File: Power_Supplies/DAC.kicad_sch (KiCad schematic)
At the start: 42 parts, among them J1 Line Out, J2 Headphone Out, U10 OPA2134, U11 TPA6110A2DGN, U9 PCM1780

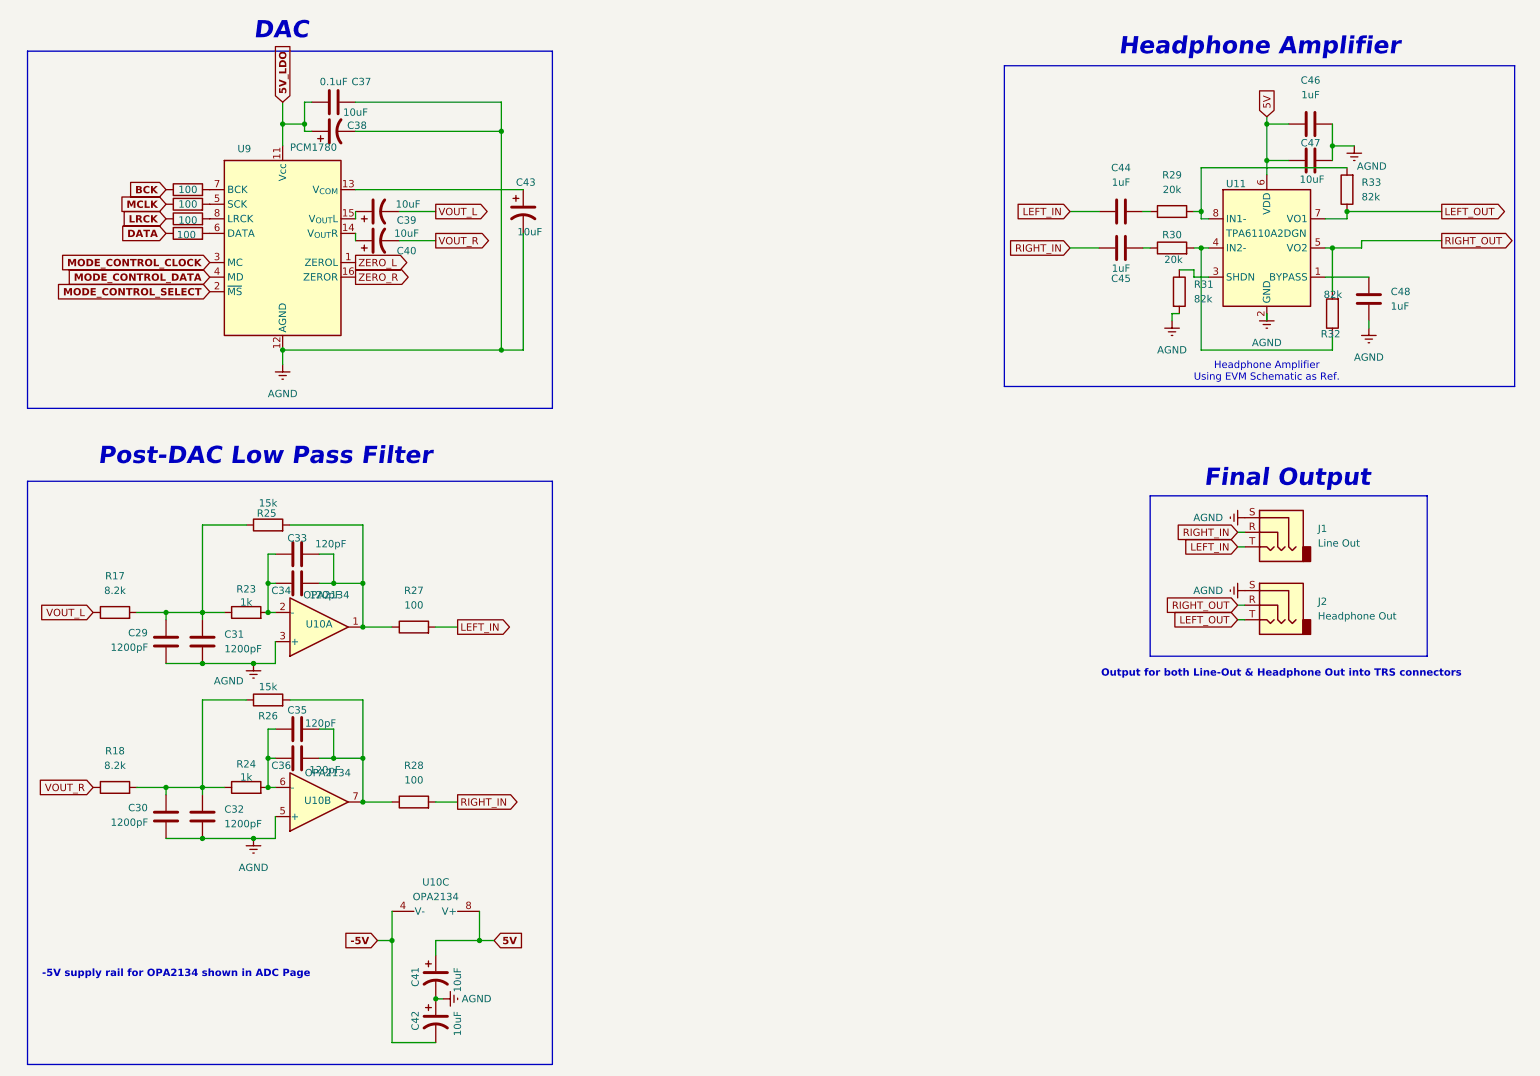
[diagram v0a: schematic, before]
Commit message: added both ADCs, added differential output to DACs
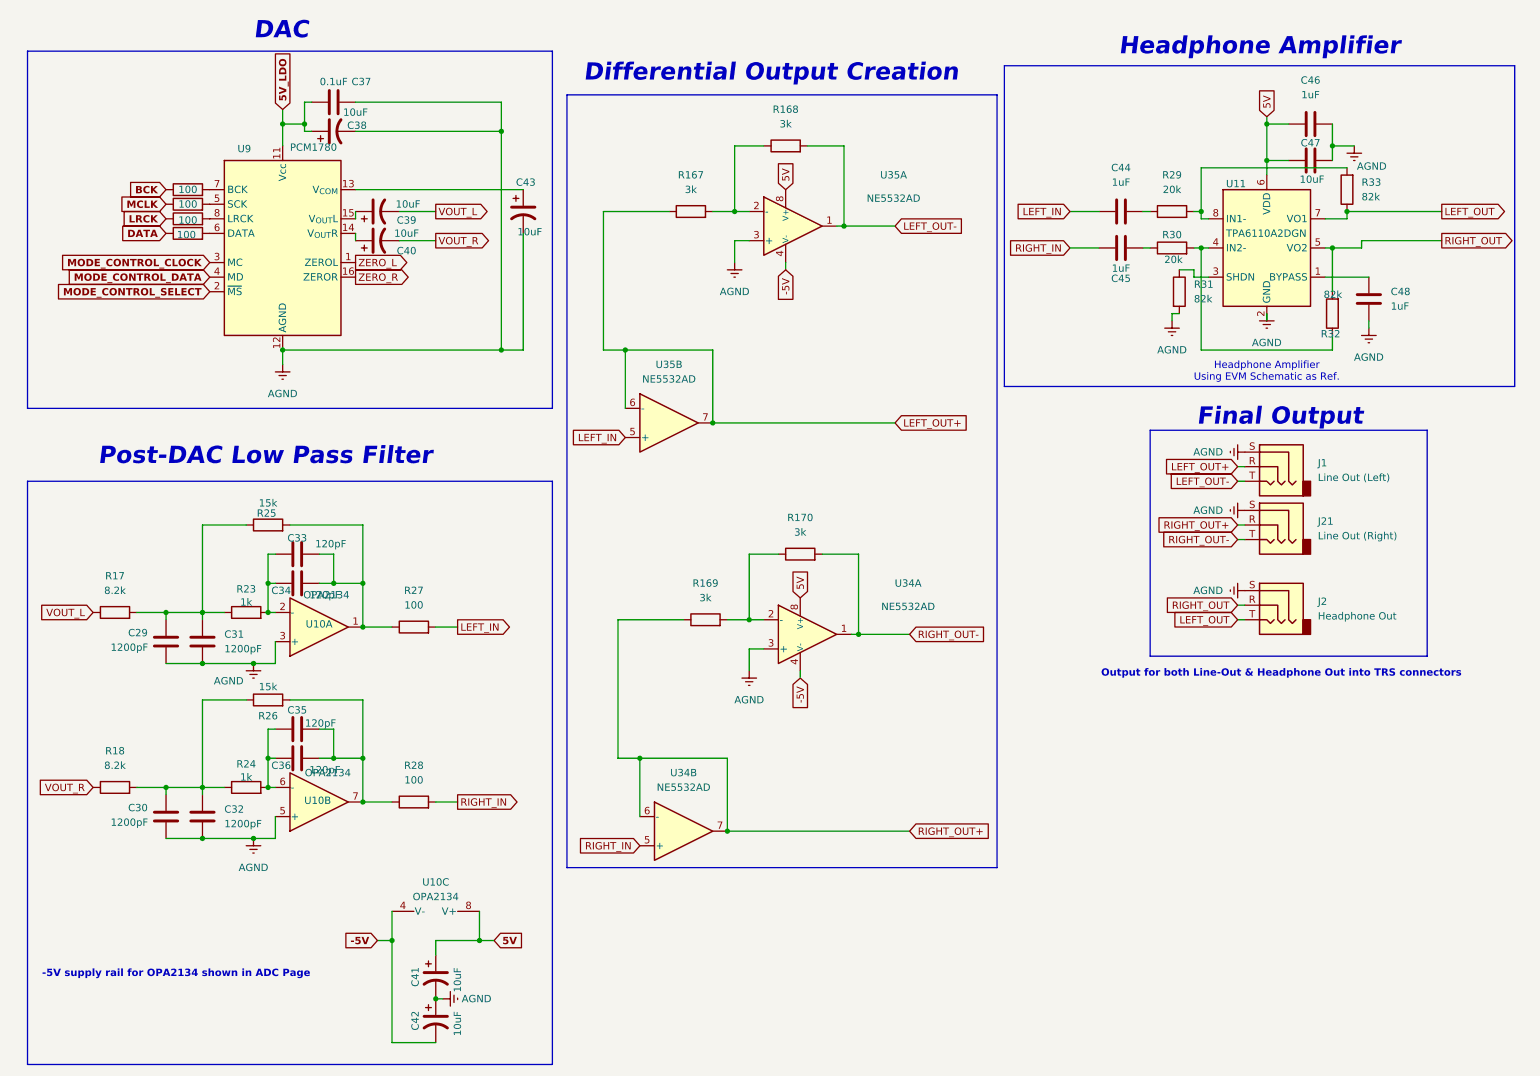
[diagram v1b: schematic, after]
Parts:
- added J21: Line Out (Right), Connector_Audio:Jack_3.5mm_CUI_SJ-3523-SMT_Horizontal, symbol Connector_Audio:AudioJack3
- added R167, R168, R169, R170: 3k, Resistor_SMD:R_0805_2012Metric, symbol Device:R
- added U34, U35: NE5532AD, PCM_Package_SO_AKL:SO-8_3.9x4.9mm_P1.27mm, symbol PCM_Amplifier_Operational_AKL:NE5532AD
- J1: value Line Out -> Line Out (Left)
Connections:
- net -5V: now also U34.4 (V-), U35.4 (V-)
- net 5V: now also U34.8 (V+), U35.8 (V+)
- net AGND: now also J21.S, U34.3 (+), U35.3 (+)
- net LEFT_IN: now also U35.5 (+); no longer J1.T
- net RIGHT_IN: now also U34.5 (+); no longer J1.R
- new net: R169.2, R170.1, U34.2 (-)
- new net: R167.2, R168.1, U35.2 (-)
- new net LEFT_OUT+: J1.R, R167.1, U35.6 (-), U35.7
- new net LEFT_OUT-: J1.T, R168.2, U35.1
- new net RIGHT_OUT+: J21.R, R169.1, U34.6 (-), U34.7
- new net RIGHT_OUT-: J21.T, R170.2, U34.1
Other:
- note added: "Differential Output Creation"
- moved on the sheet: J1

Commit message: initial placement of all cmponents
need to add:
- pin headers for Rpi
- separate the boards and add pin headers for connection points
- probably get rid of buck converters and change LDOs to be higher current
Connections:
- net LEFT_IN: now also C44.2; no longer C44.1
- net at R29.1: now also C44.1; no longer C44.2
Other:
- moved on the sheet: C44
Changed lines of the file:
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@@
 	(symbol
 		(lib_id "Device:C")
-		(at 205.74 46.99 90)
+		(at 205.74 46.99 270)
 		(unit 1)
 		(exclude_from_sim no)
@@
 		)
 		(property "Footprint" "Capacitor_SMD:C_0805_2012Metric"
-			(at 209.55 46.0248 0)
+			(at 201.93 47.9552 0)
 			(effects
 				(font

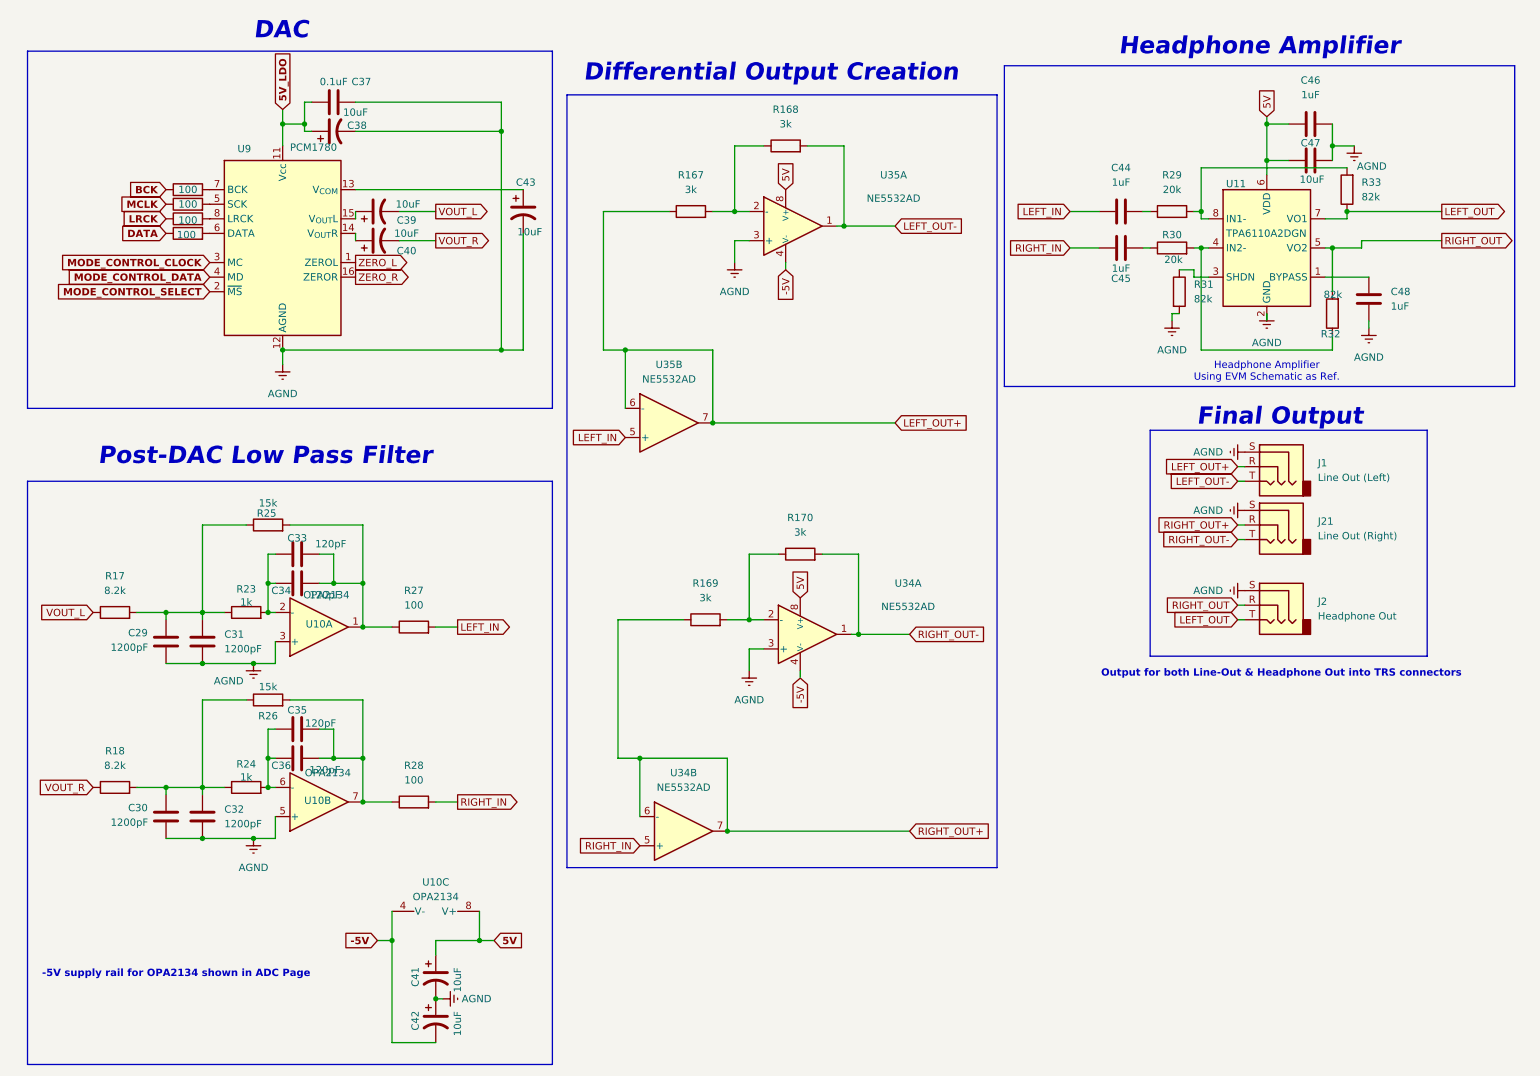
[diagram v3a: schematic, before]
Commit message: Added stuff for the power supply circuitry
changed all grounds to GND (same ground plane)
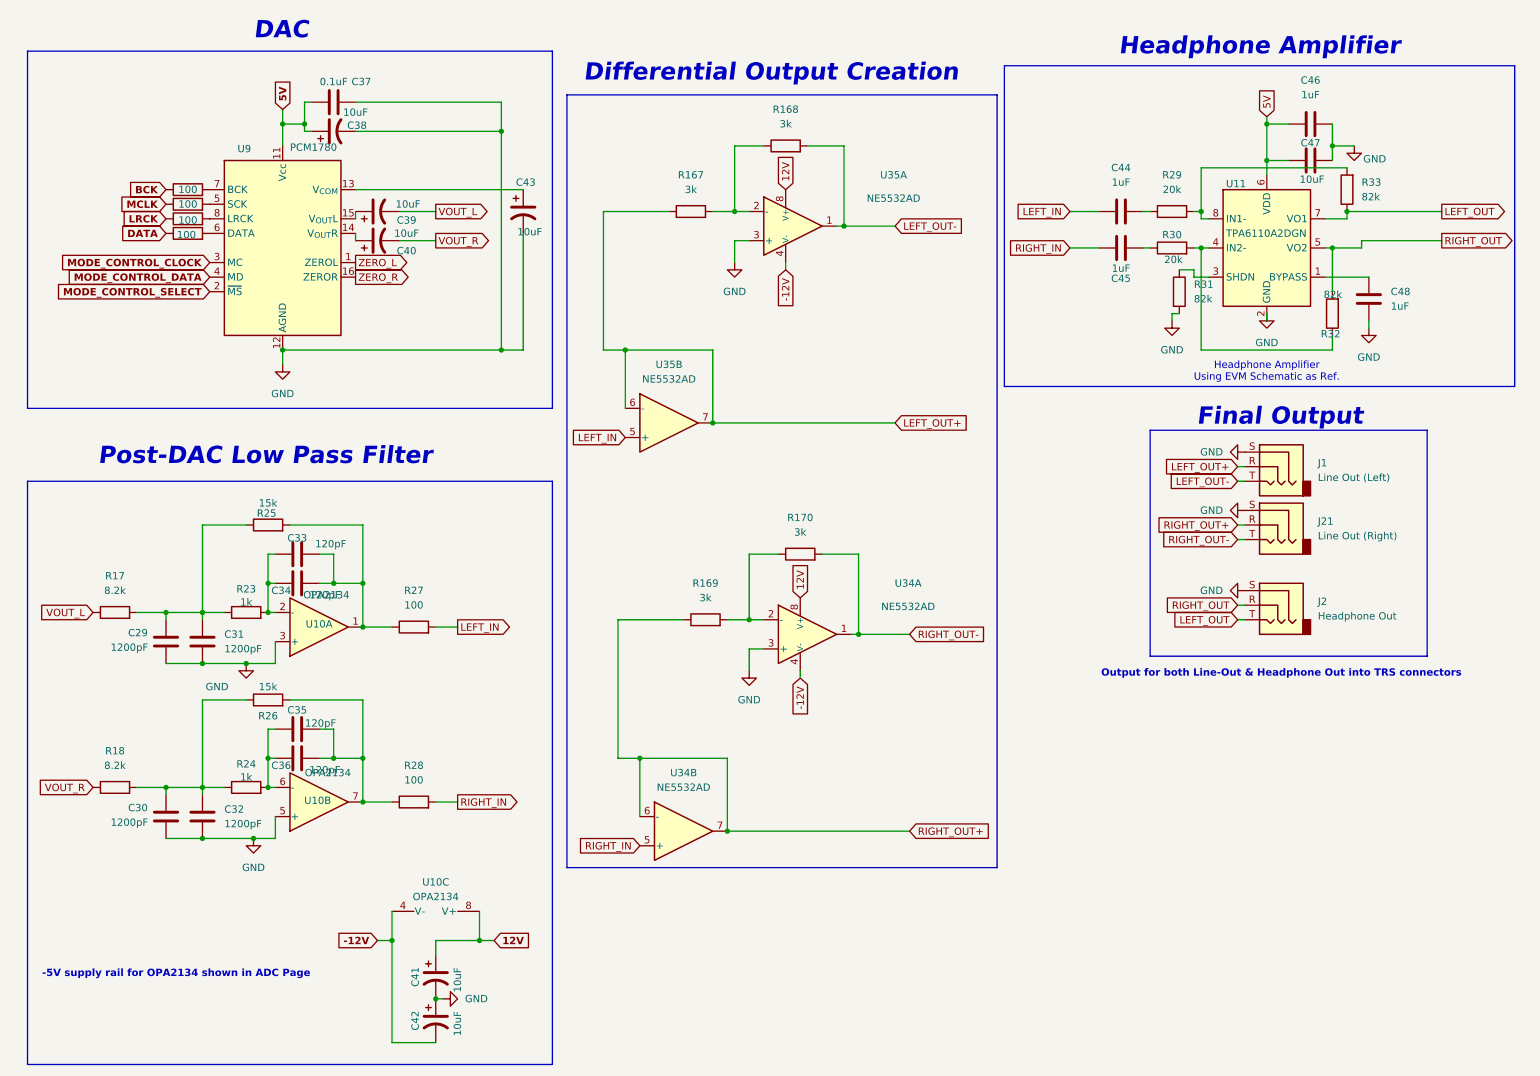
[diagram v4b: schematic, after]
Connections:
- net 5V_LDO is gone; now on net 5V: C37.1, C38.1, U9.11 (Vcc)
- net 5V: no longer C41.1, U10.8 (V+), U34.8 (V+), U35.8 (V+)
- net -5V renamed -12V
- net AGND renamed GND
- new net 12V: C41.1, U10.8 (V+), U34.8 (V+), U35.8 (V+)
